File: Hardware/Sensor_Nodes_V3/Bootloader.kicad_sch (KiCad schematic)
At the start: 33 parts, among them J1 Conn_01x04_Socket, Q1 S9013, U5 STM32F103C8Tx, Y1 8MHz

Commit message: a lot of progress on V3, still need to test if bootloader works
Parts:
- removed C14: 100nF, Capacitor_SMD:C_0402_1005Metric, symbol Device:C
- removed J1: Conn_01x04_Socket, symbol Connector:Conn_01x04_Socket
- removed JP1: ~, Jumper:SolderJumper-3_P1.3mm_Bridged12_Pad1.0x1.5mm, symbol Jumper:SolderJumper_3_Bridged12
- added J1: Conn_01x06_Socket, Connector_JST:JST_PH_B6B-PH-K_1x06_P2.00mm_Vertical, symbol Connector:Conn_01x06_Socket
- added R16, R17: 5.1k, Resistor_SMD:R_0402_1005Metric, symbol Device:R
- R11: footprint (none) -> Resistor_SMD:R_0402_1005Metric
- R12: value 100R -> 100
- R8, R9: value 220R -> 220
- Y1: footprint st-link:Crystal_SMD_5032-2Pin_5.0x3.2mm -> Crystal:Crystal_SMD_5032-2Pin_5.0x3.2mm
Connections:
- net +3V3: now also R4.2
- net D+: now also J1.4 (Pin_4)
- net D-: now also J1.3 (Pin_3)
- net GND: now also J1.1 (Pin_1), R16.2, R17.2
- net VBUS: now also J1.6 (Pin_6)
- net XTAL_S: now reaches C9.1, U5.5 (PD0), Y1.1
- new net: J1.5 (Pin_5), R17.1
- new net: J1.2 (Pin_2), R16.1
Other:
- moved on the sheet: C11, C12, C13, C15, C8, D2, D3, D4, Q1, R10, R13, R14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

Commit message: sync update
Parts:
- C10, C11, C12, C13, C15, C8, C9: footprint Capacitor_SMD:C_0402_1005Metric -> Capacitor_SMD:C_0603_1608Metric
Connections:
- net +3.3V: now also C11.1, C12.1, C13.1, C15.1, C8.1, Q1.3 (C), R8.2, TP1.1
- net +3V3: no longer C11.1, C12.1, C13.1, C15.1, C8.1, Q1.3 (C), R8.2, TP1.1
- net XTAL_S: now also C10.1, U5.6 (PD1), Y1.2; no longer C9.1, U5.5 (PD0), Y1.1
- new net: C9.1, U5.5 (PD0), Y1.1
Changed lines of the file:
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@@
 	)
 	(junction
-		(at 44.45 50.8)
-		(diameter 0)
-		(color 0 0 0 0)
-	)
-	(junction
 		(at 133.35 40.64)
 		(diameter 0)
@@
 	(wire
 		(pts
-			(xy 44.45 48.26) (xy 44.45 50.8)
-		)
-		(stroke
-			(width 0)
-			(type default)
-		)
-	)
-	(wire
-		(pts
 			(xy 222.25 140.97) (xy 224.79 140.97)
 		)
@@
 	(wire
 		(pts
-			(xy 44.45 50.8) (xy 83.82 50.8)
-		)
-		(stroke
-			(width 0)
-			(type default)
-		)
-	)
-	(wire
-		(pts
 			(xy 66.04 60.96) (xy 83.82 60.96)
 		)
@@
 	(wire
 		(pts
-			(xy 41.91 50.8) (xy 44.45 50.8)
+			(xy 41.91 50.8) (xy 83.82 50.8)
 		)
 		(stroke
@@
 		)
 	)
-	(global_label "XTAL_S"
-		(shape input)
-		(at 44.45 48.26 0)
-		(fields_autoplaced yes)
-		(effects
-			(font
-				(size 1.27 1.27)
-			)
-			(justify left)
-		)
-		(property "Intersheetrefs" "${INTERSHEET_REFS}"
-			(at 53.9061 48.26 0)
-			(effects
-				(font
-					(size 1.27 1.27)
-				)
-				(justify left)
-				(hide yes)
-			)
-		)
-	)
 	(global_label "T_CLK"
 		(shape input)
@@
 		)
 	)
+	(global_label "XTAL_S"
+		(shape input)
+		(at 54.61 57.15 0)
+		(fields_autoplaced yes)
+		(effects
+			(font
+				(size 1.27 1.27)
+			)
+			(justify left)
+		)
+		(property "Intersheetrefs" "${INTERSHEET_REFS}"
+			(at 64.0661 57.15 0)
+			(effects
+				(font
+					(size 1.27 1.27)
+				)
+				(justify left)
+				(hide yes)
+			)
+		)
+	)
 	(global_label "LED"
 		(shape input)
@@
 		)
 		(property "Intersheetrefs" "${INTERSHEET_REFS}"
-			(at 122.0134 68.58 0)
+			(at 122.6676 68.58 0)
 			(effects
 				(font
@@
 			)
 		)
-		(property "Value" "+3V3"
+		(property "Value" "+3.3V"
 			(at 166.751 164.5158 0)
 			(effects
@@
 			)
 		)
-		(property "Value" "+3V3"
+		(property "Value" "+3.3V"
 			(at 227.711 32.4358 0)
 			(effects
@@
 			)
 		)
-		(property "Value" "+3V3"
+		(property "Value" "+3.3V"
 			(at 212.471 23.5458 0)
 			(effects
@@
 			)
 		)
-		(property "Footprint" "Capacitor_SMD:C_0402_1005Metric"
+		(property "Footprint" "Capacitor_SMD:C_0603_1608Metric"
 			(at 55.5752 69.85 0)
 			(effects
@@
 			)
 		)
-		(property "Value" "+3V3"
+		(property "Value" "+3.3V"
 			(at 245.491 107.3658 0)
 			(effects
@@
 			)
 		)
-		(property "Footprint" "Capacitor_SMD:C_0402_1005Metric"
+		(property "Footprint" "Capacitor_SMD:C_0603_1608Metric"
 			(at 234.6452 46.99 0)
 			(effects
@@
 			)
 		)
-		(property "Footprint" "Capacitor_SMD:C_0402_1005Metric"
+		(property "Footprint" "Capacitor_SMD:C_0603_1608Metric"
 			(at 260.0452 46.99 0)
 			(effects
@@
 			)
 		)
-		(property "Footprint" "Capacitor_SMD:C_0402_1005Metric"
+		(property "Footprint" "Capacitor_SMD:C_0603_1608Metric"
 			(at 228.2952 46.99 0)
 			(effects
@@
 			)
 		)
-		(property "Footprint" "Capacitor_SMD:C_0402_1005Metric"
+		(property "Footprint" "Capacitor_SMD:C_0603_1608Metric"
 			(at 240.9952 46.99 0)
 			(effects
@@
 			)
 		)
-		(property "Footprint" "Capacitor_SMD:C_0402_1005Metric"
+		(property "Footprint" "Capacitor_SMD:C_0603_1608Metric"
 			(at 42.8752 69.85 0)
 			(effects
@@
 			)
 		)
-		(property "Footprint" "Capacitor_SMD:C_0402_1005Metric"
+		(property "Footprint" "Capacitor_SMD:C_0603_1608Metric"
 			(at 247.3452 46.99 0)
 			(effects

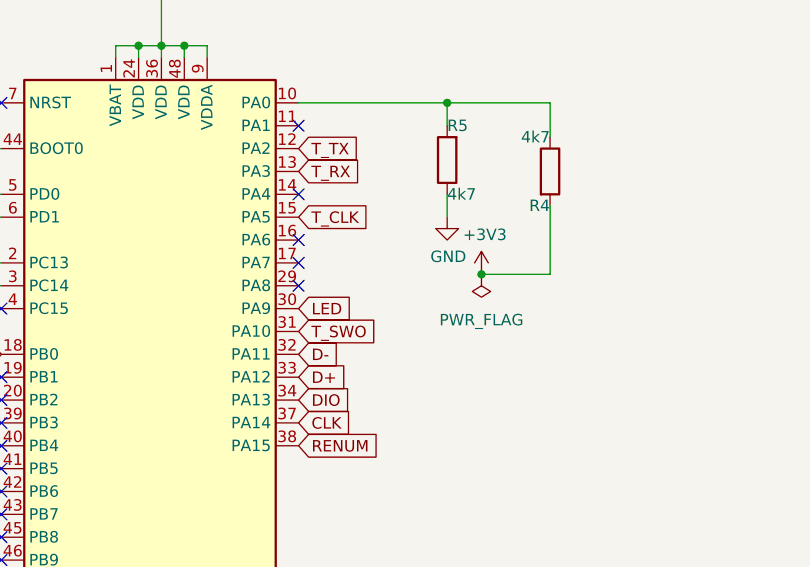
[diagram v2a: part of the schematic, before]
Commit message: finished v3, need to fix drc silkscreens
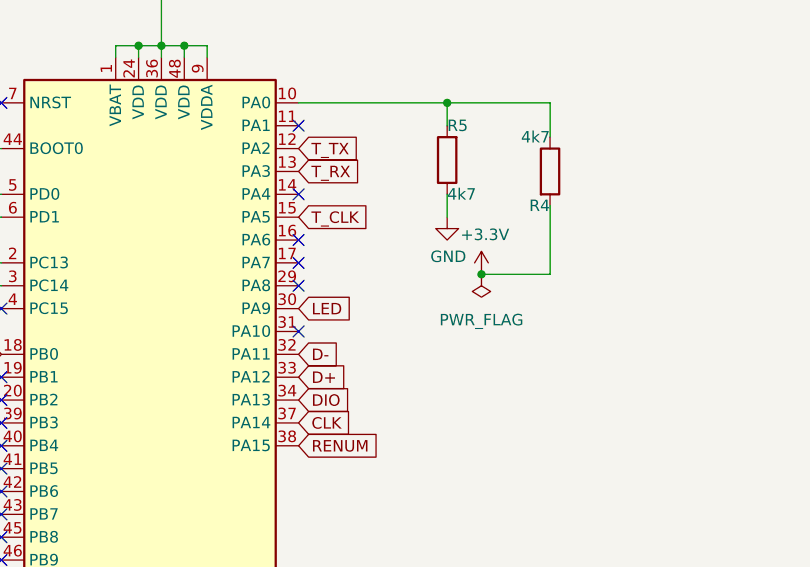
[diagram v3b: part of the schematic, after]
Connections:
- net +3V3 is gone; now on net +3.3V: R4.2
- net T_SWO: no longer names the net of U5.31 (PA10)
- no-connect marks 19 -> 20
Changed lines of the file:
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@@
 	)
 	(no_connect
+		(at 116.84 66.04)
+	)
+	(no_connect
 		(at 116.84 50.8)
 	)
@@
 		)
 	)
-	(global_label "T_SWO"
-		(shape input)
-		(at 116.84 66.04 0)
-		(fields_autoplaced yes)
-		(effects
-			(font
-				(size 1.27 1.27)
-			)
-			(justify left)
-		)
-		(property "Intersheetrefs" "${INTERSHEET_REFS}"
-			(at 125.0976 66.04 0)
-			(effects
-				(font
-					(size 1.27 1.27)
-				)
-				(justify left)
-				(hide yes)
-			)
-		)
-	)
 	(global_label "DIO"
 		(shape input)
@@
 			)
 		)
-		(property "Value" "+3V3"
+		(property "Value" "+3.3V"
 			(at 137.541 55.2958 0)
 			(effects

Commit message: finished the thing, need to optimize bom a little bit. need to flip some of the components too
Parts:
- C10, C9: LCSC C1554 -> C1648
- C11, C12, C13, C8: LCSC C1525 -> C14663
- C15: LCSC C1525 -> C19666
- R11: LCSC (none) -> C25741
- R15: value 100R -> 100
- R16, R17: LCSC (none) -> C25905
- U5: LCSC (none) -> C8734
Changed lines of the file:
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@@
 	)
 	(junction
-		(at 137.16 59.69)
-		(diameter 0)
-		(color 0 0 0 0)
-	)
-	(junction
 		(at 240.03 48.26)
 		(diameter 0)
@@
 			)
 		)
-		(property "LCSC" "C1554"
+		(property "LCSC" "C1648"
 			(at 54.61 66.04 0)
 			(effects
@@
 			)
 		)
+		(property "LCSC" "C25905"
+			(at 209.55 143.51 0)
+			(effects
+				(font
+					(size 1.27 1.27)
+				)
+				(hide yes)
+			)
+		)
 		(pin "1"
 		)
@@
 			)
 		)
+		(property "LCSC" "C8734"
+			(at 99.06 76.2 0)
+			(effects
+				(font
+					(size 1.27 1.27)
+				)
+				(hide yes)
+			)
+		)
 		(pin "37"
 		)
@@
 			)
 		)
+		(property "LCSC" "C25905"
+			(at 209.55 151.13 0)
+			(effects
+				(font
+					(size 1.27 1.27)
+				)
+				(hide yes)
+			)
+		)
 		(pin "1"
 		)
@@
 			)
 		)
-		(property "Value" "100R"
+		(property "Value" "100"
 			(at 266.7 123.19 90)
 			(effects
@@
 	)
 	(symbol
-		(lib_id "power:PWR_FLAG")
-		(at 137.16 59.69 180)
-		(unit 1)
-		(exclude_from_sim no)
-		(in_bom yes)
-		(on_board yes)
-		(dnp no)
-		(fields_autoplaced yes)
-		(property "Reference" "#FLG05"
-			(at 137.16 61.595 0)
-			(effects
-				(font
-					(size 1.27 1.27)
-				)
-				(hide yes)
-			)
-		)
-		(property "Value" "PWR_FLAG"
-			(at 137.16 64.77 0)
-			(effects
-				(font
-					(size 1.27 1.27)
-				)
-			)
-		)
-		(property "Footprint" ""
-			(at 137.16 59.69 0)
-			(effects
-				(font
-					(size 1.27 1.27)
-				)
-				(hide yes)
-			)
-		)
-		(property "Datasheet" "~"
-			(at 137.16 59.69 0)
-			(effects
-				(font
-					(size 1.27 1.27)
-				)
-				(hide yes)
-			)
-		)
-		(property "Description" "Special symbol for telling ERC where power comes from"
-			(at 137.16 59.69 0)
-			(effects
-				(font
-					(size 1.27 1.27)
-				)
-				(hide yes)
-			)
-		)
-		(pin "1"
-		)
-		(instances
-			(project ""
-				(path "/7b4e8e38-4440-451f-8c12-a5c49d6e3525/ef5be6a6-6fd2-4813-9489-058ffa5a3841"
-					(reference "#FLG05")
-					(unit 1)
-				)
-			)
-		)
-	)
-	(symbol
 		(lib_id "power:GND")
 		(at 60.96 72.39 0)
@@
 			)
 		)
+		(property "LCSC" "C25741"
+			(at 34.29 50.8 0)
+			(effects
+				(font
+					(size 1.27 1.27)
+				)
+				(hide yes)
+			)
+		)
 		(pin "1"
 		)
@@
 			)
 		)
-		(property "LCSC" "C1525"
+		(property "LCSC" "C14663"
 			(at 233.68 43.18 0)
 			(effects
@@
 			)
 		)
-		(property "LCSC" "C1525"
+		(property "LCSC" "C19666"
 			(at 259.08 43.18 0)
 			(effects
@@
 			)
 		)
-		(property "LCSC" "C1525"
+		(property "LCSC" "C14663"
 			(at 227.33 43.18 0)
 			(effects
@@
 			)
 		)
-		(property "LCSC" "C1525"
+		(property "LCSC" "C14663"
 			(at 240.03 43.18 0)
 			(effects
@@
 			)
 		)
-		(property "LCSC" "C1554"
+		(property "LCSC" "C1648"
 			(at 41.91 66.04 0)
 			(effects
@@
 			)
 		)
-		(property "LCSC" "C1525"
+		(property "LCSC" "C14663"
 			(at 246.38 43.18 0)
 			(effects

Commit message: alt placement made
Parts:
- removed R16, R17: 5.1k, Resistor_SMD:R_0402_1005Metric, symbol Device:R
- added R10, R7: 5.1k, Resistor_SMD:R_0402_1005Metric, symbol Device:R
- R4: renamed from R12; footprint Resistor_SMD:R_0402_1005Metric -> Resistor_SMD:R_0603_1608Metric; LCSC C25076 -> C22775
- renumbered C9 to C1, C10 to C2, C8 to C3, C11 to C4, C12 to C5, C13 to C6, C15 to C7, D2 to D1, D3 to D2, D4 to D3, R11 to R1, R10 to R11, R13 to R12, R14 to R13, R15 to R14, R6 to R2, R7 to R3, R4 to R6, TP1 to T1, TP2 to T2, TP3 to T3, TP4 to T4, TP5 to T5, U5 to U1
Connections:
- net D+: now also J1.2 (Pin_2); no longer J1.4 (Pin_4)
- net D-: now also J1.5 (Pin_5); no longer J1.3 (Pin_3)
- net GND: now also R10.2, R7.2
- new net: J1.3 (Pin_3), R10.1
- new net: J1.4 (Pin_4), R7.1

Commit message: rerouted a little and added swo
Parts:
- added T6, T7, T8: ~, TestPoint:TestPoint_Pad_1.0x1.0mm, symbol Connector:TestPoint
- D1: LCSC C72041 -> C2290
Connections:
- net T_CLK: now also T7.1
- net T_DIO: now also T6.1
- net T_SWO: now reaches U1.31 (PA10)
- net T_SWO: now also T8.1
- no-connect marks 20 -> 19

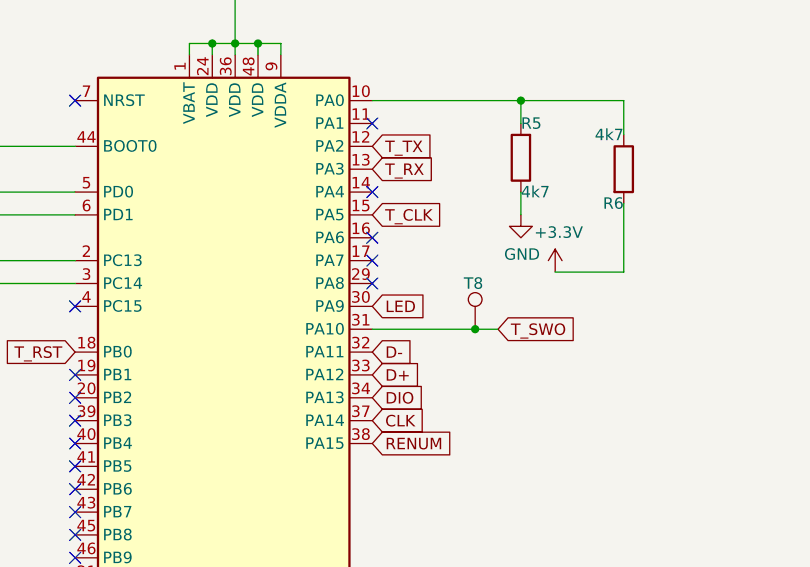
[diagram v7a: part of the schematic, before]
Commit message: fixed placement, added some decals, now using clock from stlink
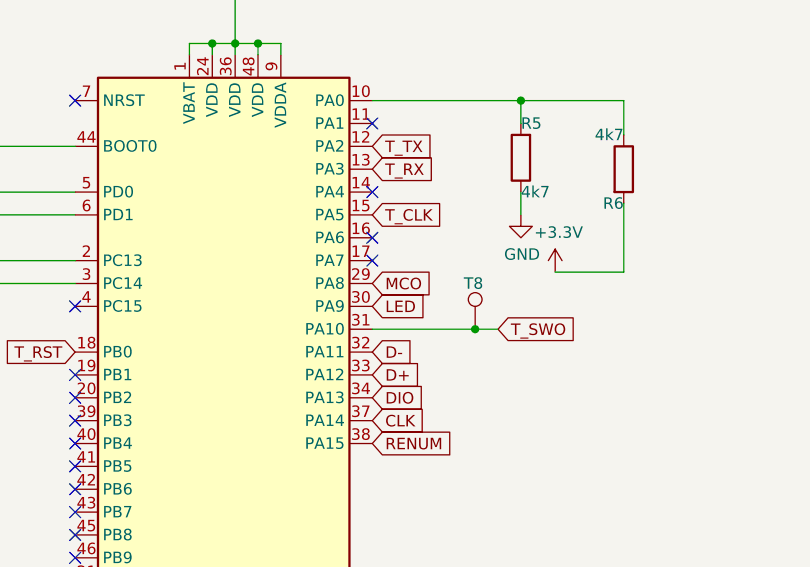
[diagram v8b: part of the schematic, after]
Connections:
- net MCO: now reaches U1.29 (PA8)
- no-connect marks 19 -> 18
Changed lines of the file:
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@@
-	)
-	(no_connect
-		(at 116.84 60.96)
 	)
 	(no_connect
@@
 				(hide yes)
 			)
+		)
+	)
+	(global_label "MCO"
+		(shape input)
+		(at 116.84 60.96 0)
+		(fields_autoplaced yes)
+		(effects
+			(font
+				(size 1.27 1.27)
+			)
+			(justify left)
+		)
+		(property "Intersheetrefs" "${INTERSHEET_REFS}"
+			(at 123.8771 60.96 0)
+			(effects
+				(font
+					(size 1.27 1.27)
+				)
+				(justify left)
+				(hide yes)
+			)
